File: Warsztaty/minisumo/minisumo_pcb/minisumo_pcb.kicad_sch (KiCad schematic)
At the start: 0 parts

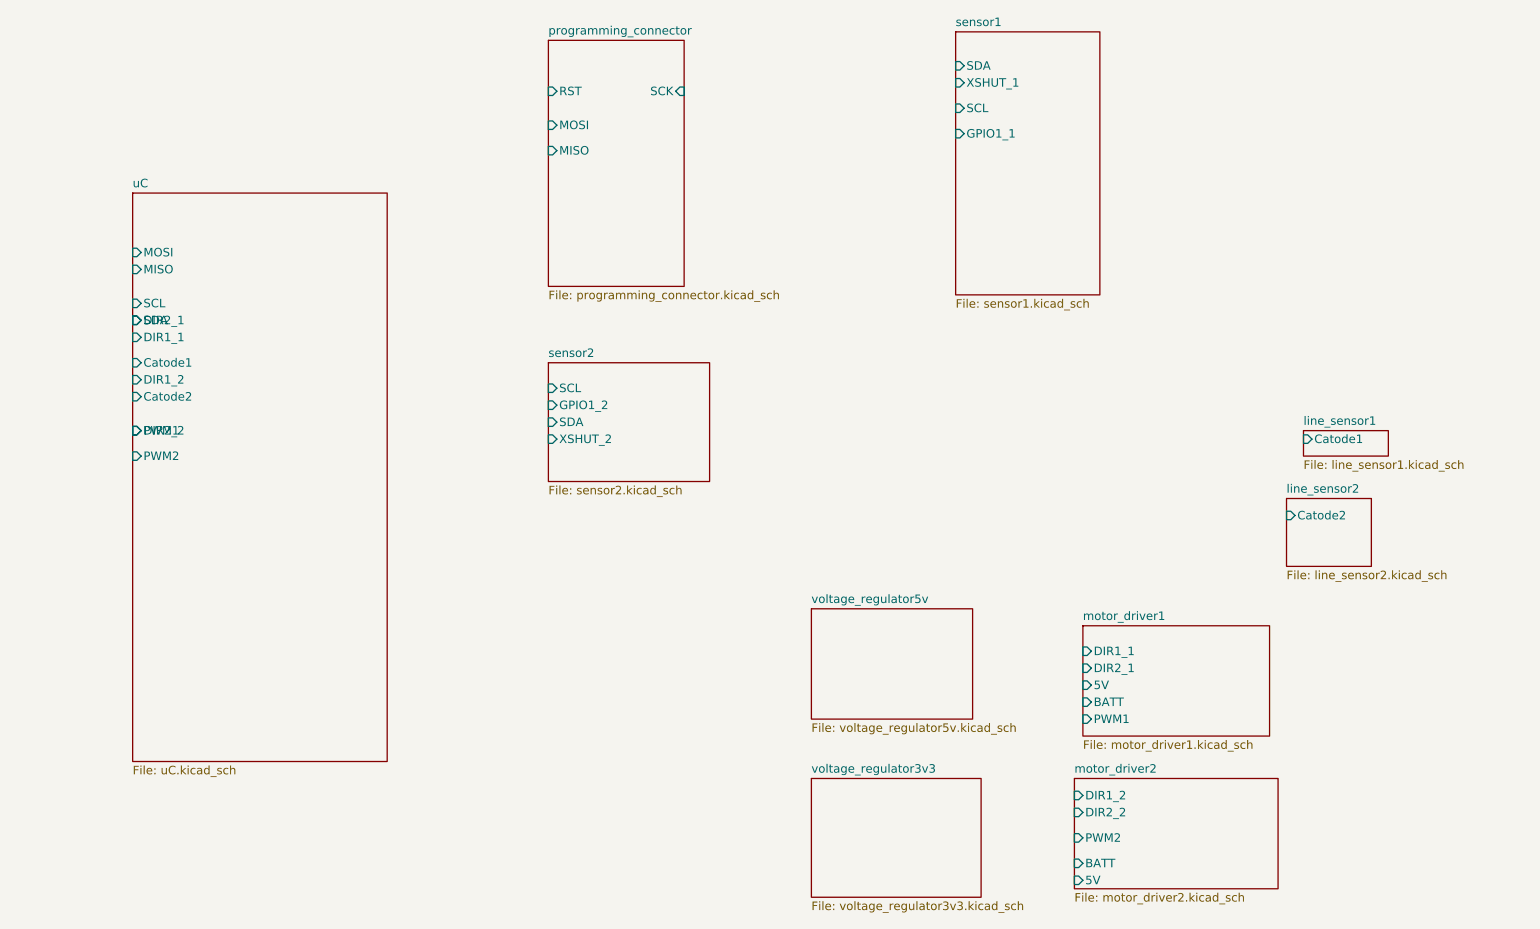
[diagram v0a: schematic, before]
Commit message: laczenie hierarchiczne schematu
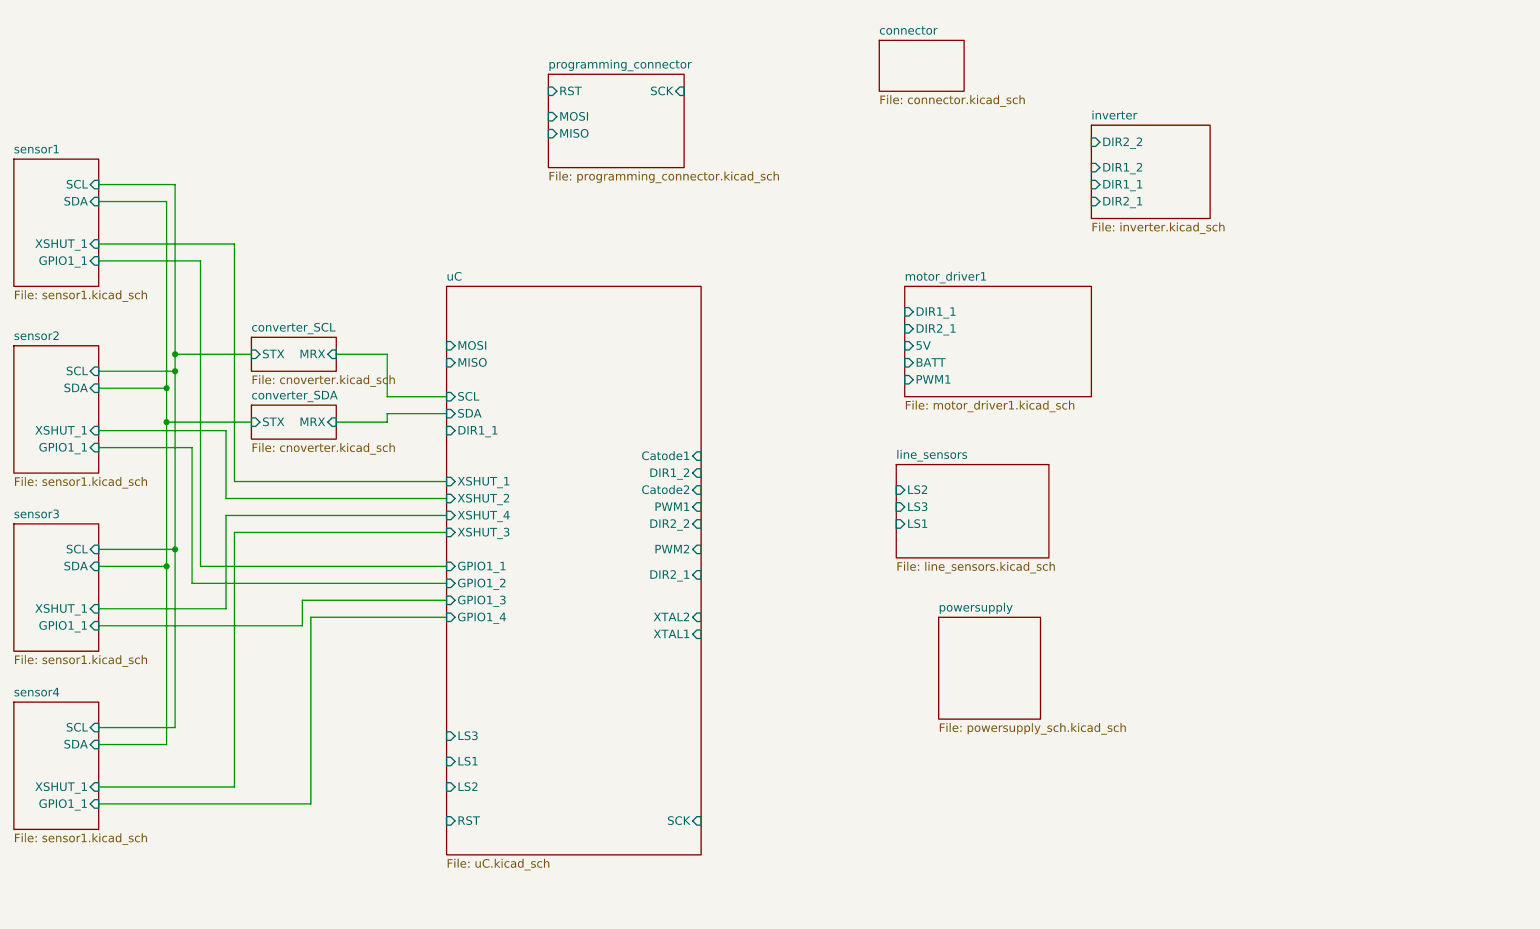
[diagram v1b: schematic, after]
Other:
- removed sheet line_sensor1
- removed sheet line_sensor2
- removed sheet motor_driver2
- removed sheet voltage_regulator3v3
- removed sheet voltage_regulator5v
- added sheet connector (connector.kicad_sch)
- added sheet converter_SCL (cnoverter.kicad_sch)
- added sheet converter_SDA (cnoverter.kicad_sch)
- added sheet inverter (inverter.kicad_sch)
- added sheet line_sensors (line_sensors.kicad_sch)
- added sheet powersupply (powersupply_sch.kicad_sch)
- added sheet sensor3 (sensor1.kicad_sch)
- added sheet sensor4 (sensor1.kicad_sch)
- sheet sensor2: file sensor2.kicad_sch -> sensor1.kicad_sch
- sheet sensor2 ports: added GPIO1_1, XSHUT_1; removed GPIO1_2, XSHUT_2
- sheet uC ports: added GPIO1_1, GPIO1_2, GPIO1_3, GPIO1_4, LS1, LS2, LS3, RST, SCK, XSHUT_1, XSHUT_2, XSHUT_3, XSHUT_4, XTAL1, XTAL2; removed none

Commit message: wstepnie skonczony schemat
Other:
- removed sheet connector
- added sheet converter_GPIO1_1 (cnoverter.kicad_sch)
- added sheet converter_GPIO1_2 (cnoverter.kicad_sch)
- added sheet converter_GPIO1_4 (cnoverter.kicad_sch)
- added sheet converter_XSHUT_1 (cnoverter.kicad_sch)
- added sheet converter_XSHUT_2 (cnoverter.kicad_sch)
- added sheet converter_XSHUT_3 (cnoverter.kicad_sch)
- added sheet converter_XSHUT_4 (cnoverter.kicad_sch)
- added sheet motor_driver2 (motor_driver1.kicad_sch)
- sheet motor_driver1 ports: added none; removed 5V, BATT
- sheet uC ports: added none; removed Catode1, Catode2, DIR1_1, DIR2_1
